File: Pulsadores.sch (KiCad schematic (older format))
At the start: 14 parts, among them SW1 Izquierda, SW2 Arriba, SW3 Abajo, SW4 Derecha, U6 74HC148

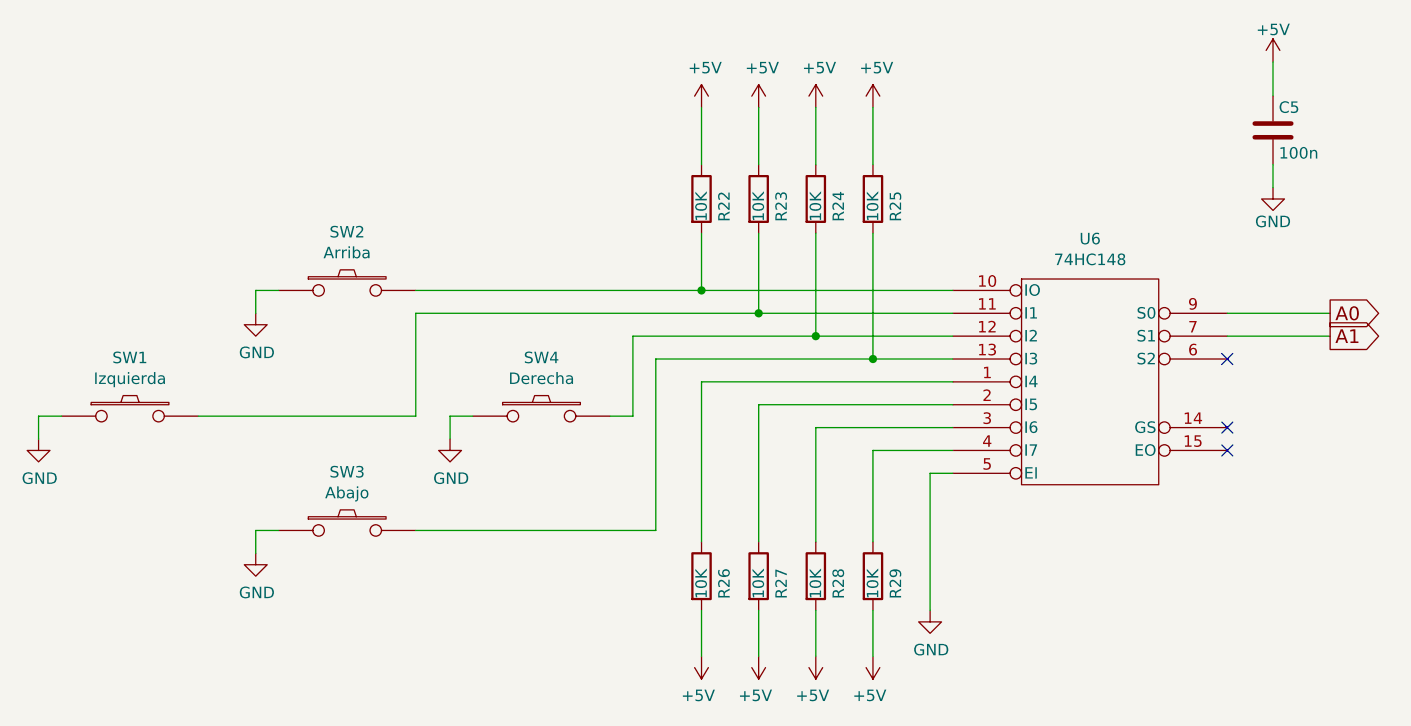
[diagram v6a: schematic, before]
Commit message: añadidos driver para led y conectores para fotodiodos infrarrojos
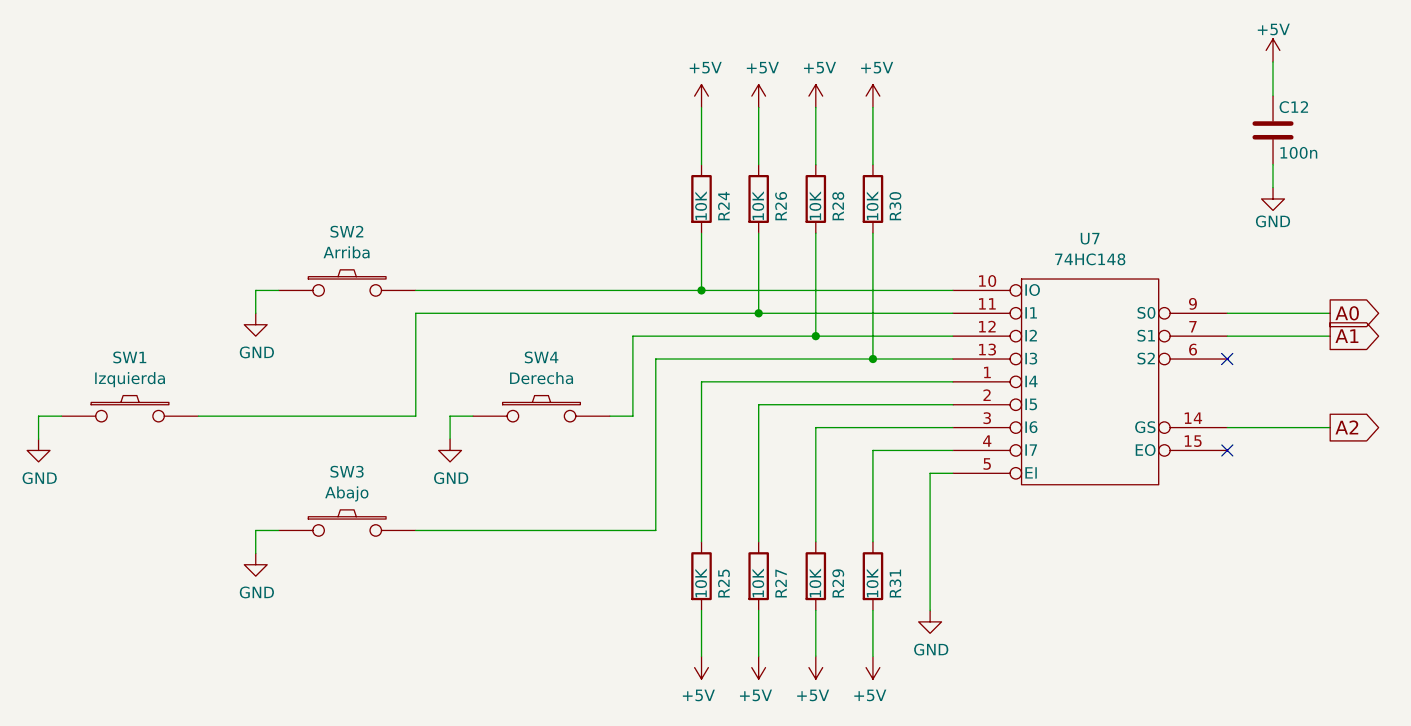
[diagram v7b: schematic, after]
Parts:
- renumbered C5 to C12, R22 to R24, R26 to R25, R23 to R26, R24 to R28, R28 to R29, R25 to R30, R29 to R31, U6 to U7
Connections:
- net A2: now reaches U7.14 (GS)
- no-connect marks 3 -> 2
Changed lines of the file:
@@
 EESchema Schematic File Version 2
+LIBS:Interfaces
+LIBS:Nano_PB-rescue
 LIBS:Sensores
 LIBS:power
@@
 LIBS:valves
 LIBS:MyLibrary
+LIBS:matriz_led
 LIBS:Nano_PB-cache
-EELAYER 25 0
+EELAYER 26 0
 EELAYER END
 $Descr User 8268 5846
 encoding utf-8
-Sheet 11 15
+Sheet 11 16
 Title "Bloque de pulsadores"
-Date "2016-08-07"
-Rev "V.0.2"
+Date "2017-01-04"
+Rev "V.0.3"
 Comp "NanoPlayBoard"
 Comment1 "Creada por Antonio Morales"
@@
 $EndDescr
 $Comp
-L 74LS148 U6
+L 74LS148 U7
 U 1 1 5793F705
 P 5650 2450
-F 0 "U6" H 5650 3075 50  0000 C CNN
+F 0 "U7" H 5650 3075 50  0000 C CNN
 F 1 "74HC148" H 5650 2984 50  0000 C CNN
 F 2 "Housings_SOIC:SOIC-16_3.9x9.9mm_Pitch1.27mm" H 5650 2450 50  0001 C CNN
@@
 	1050 2600 1050 2700
 $Comp
-L GND #PWR030
+L GND #PWR051
 U 1 1 57951274
 P 1050 2700
-F 0 "#PWR030" H 1050 2450 50  0001 C CNN
+F 0 "#PWR051" H 1050 2450 50  0001 C CNN
 F 1 "GND" H 1055 2527 50  0000 C CNN
 F 2 "" H 1050 2700 50  0000 C CNN
@@
 	2000 3100 2000 3200
 $Comp
-L GND #PWR031
+L GND #PWR052
 U 1 1 579512A4
 P 2000 3200
-F 0 "#PWR031" H 2000 2950 50  0001 C CNN
+F 0 "#PWR052" H 2000 2950 50  0001 C CNN
 F 1 "GND" H 2005 3027 50  0000 C CNN
 F 2 "" H 2000 3200 50  0000 C CNN
@@
 	2000 2050 2000 2150
 $Comp
-L GND #PWR032
+L GND #PWR053
 U 1 1 579512CF
 P 2000 2150
-F 0 "#PWR032" H 2000 1900 50  0001 C CNN
+F 0 "#PWR053" H 2000 1900 50  0001 C CNN
 F 1 "GND" H 2005 1977 50  0000 C CNN
 F 2 "" H 2000 2150 50  0000 C CNN
@@
 	2850 2600 2850 2700
 $Comp
-L GND #PWR033
+L GND #PWR054
 U 1 1 5795130B
 P 2850 2700
-F 0 "#PWR033" H 2850 2450 50  0001 C CNN
+F 0 "#PWR054" H 2850 2450 50  0001 C CNN
 F 1 "GND" H 2855 2527 50  0000 C CNN
 F 2 "" H 2850 2700 50  0000 C CNN
@@
 	2700 3100 3750 3100
 $Comp
-L R R22
+L R R24
 U 1 1 57951783
 P 3950 1650
-F 0 "R22" V 4050 1550 50  0000 L CNN
+F 0 "R24" V 4050 1550 50  0000 L CNN
 F 1 "10K" V 3950 1550 50  0000 L CNN
 F 2 "Resistencias:R_0805" V 3880 1650 50  0001 C CNN
@@
 $EndComp
 $Comp
-L R R23
+L R R26
 U 1 1 579517BD
 P 4200 1650
-F 0 "R23" V 4300 1550 50  0000 L CNN
+F 0 "R26" V 4300 1550 50  0000 L CNN
 F 1 "10K" V 4200 1550 50  0000 L CNN
 F 2 "Resistencias:R_0805" V 4130 1650 50  0001 C CNN
@@
 $EndComp
 $Comp
-L R R24
+L R R28
 U 1 1 579517EC
 P 4450 1650
-F 0 "R24" V 4550 1550 50  0000 L CNN
+F 0 "R28" V 4550 1550 50  0000 L CNN
 F 1 "10K" V 4450 1550 50  0000 L CNN
 F 2 "Resistencias:R_0805" V 4380 1650 50  0001 C CNN
@@
 $EndComp
 $Comp
-L R R25
+L R R30
 U 1 1 5795181A
 P 4700 1650
-F 0 "R25" V 4800 1550 50  0000 L CNN
+F 0 "R30" V 4800 1550 50  0000 L CNN
 F 1 "10K" V 4700 1550 50  0000 L CNN
 F 2 "Resistencias:R_0805" V 4630 1650 50  0001 C CNN
@@
 	3950 1500 3950 1250
 $Comp
-L +5V #PWR034
+L +5V #PWR055
 U 1 1 5795193F
 P 3950 1250
-F 0 "#PWR034" H 3950 1100 50  0001 C CNN
+F 0 "#PWR055" H 3950 1100 50  0001 C CNN
 F 1 "+5V" H 3965 1423 50  0000 C CNN
 F 2 "" H 3950 1250 50  0000 C CNN
@@
 $EndComp
 $Comp
-L +5V #PWR035
+L +5V #PWR056
 U 1 1 5795196C
 P 4200 1250
-F 0 "#PWR035" H 4200 1100 50  0001 C CNN
+F 0 "#PWR056" H 4200 1100 50  0001 C CNN
 F 1 "+5V" H 4215 1423 50  0000 C CNN
 F 2 "" H 4200 1250 50  0000 C CNN
@@
 $EndComp
 $Comp
-L +5V #PWR036
+L +5V #PWR057
 U 1 1 57951992
 P 4450 1250
-F 0 "#PWR036" H 4450 1100 50  0001 C CNN
+F 0 "#PWR057" H 4450 1100 50  0001 C CNN
 F 1 "+5V" H 4465 1423 50  0000 C CNN
 F 2 "" H 4450 1250 50  0000 C CNN
@@
 $EndComp
 $Comp
-L +5V #PWR037
+L +5V #PWR058
 U 1 1 579519B8
 P 4700 1250
-F 0 "#PWR037" H 4700 1100 50  0001 C CNN
+F 0 "#PWR058" H 4700 1100 50  0001 C CNN
 F 1 "+5V" H 4715 1423 50  0000 C CNN
 F 2 "" H 4700 1250 50  0000 C CNN
@@
 Wire Wire Line
 	4200 1250 4200 1500
-NoConn ~ 6250 2650
 NoConn ~ 6250 2750
 Wire Wire Line
@@
 Text GLabel 6700 2250 2    60   Output ~ 0
 A1
-NoConn ~ 6250 2350
-$Comp
-L R R26
+$Comp
+L R R25
 U 1 1 579521A8
 P 3950 3300
-F 0 "R26" V 4050 3200 50  0000 L CNN
+F 0 "R25" V 4050 3200 50  0000 L CNN
 F 1 "10K" V 3950 3200 50  0000 L CNN
 F 2 "Resistencias:R_0805" V 3880 3300 50  0001 C CNN
@@
 $EndComp
 $Comp
-L R R28
+L R R29
 U 1 1 57952253
 P 4450 3300
-F 0 "R28" V 4550 3200 50  0000 L CNN
+F 0 "R29" V 4550 3200 50  0000 L CNN
 F 1 "10K" V 4450 3200 50  0000 L CNN
 F 2 "Resistencias:R_0805" V 4380 3300 50  0001 C CNN
@@
 $EndComp
 $Comp
-L R R29
+L R R31
 U 1 1 5795229D
 P 4700 3300
-F 0 "R29" V 4800 3200 50  0000 L CNN
+F 0 "R31" V 4800 3200 50  0000 L CNN
 F 1 "10K" V 4700 3200 50  0000 L CNN
 F 2 "Resistencias:R_0805" V 4630 3300 50  0001 C CNN
@@
 	3950 3450 3950 3650
 $Comp
-L +5V #PWR038
+L +5V #PWR059
 U 1 1 579524C5
 P 3950 3650
-F 0 "#PWR038" H 3950 3500 50  0001 C CNN
+F 0 "#PWR059" H 3950 3500 50  0001 C CNN
 F 1 "+5V" H 3965 3823 50  0000 C CNN
 F 2 "" H 3950 3650 50  0000 C CNN
@@
 $EndComp
 $Comp
-L +5V #PWR039
+L +5V #PWR060
 U 1 1 57952518
 P 4200 3650
-F 0 "#PWR039" H 4200 3500 50  0001 C CNN
+F 0 "#PWR060" H 4200 3500 50  0001 C CNN
 F 1 "+5V" H 4215 3823 50  0000 C CNN
 F 2 "" H 4200 3650 50  0000 C CNN
@@
 $EndComp
 $Comp
-L +5V #PWR040
+L +5V #PWR061
 U 1 1 5795254A
 P 4450 3650
-F 0 "#PWR040" H 4450 3500 50  0001 C CNN
+F 0 "#PWR061" H 4450 3500 50  0001 C CNN
 F 1 "+5V" H 4465 3823 50  0000 C CNN
 F 2 "" H 4450 3650 50  0000 C CNN
@@
 $EndComp
 $Comp
-L +5V #PWR041
+L +5V #PWR062
 U 1 1 5795257C
 P 4700 3650
-F 0 "#PWR041" H 4700 3500 50  0001 C CNN
+F 0 "#PWR062" H 4700 3500 50  0001 C CNN
 F 1 "+5V" H 4715 3823 50  0000 C CNN
 F 2 "" H 4700 3650 50  0000 C CNN
@@
 	4950 2850 4950 3450
 $Comp
-L GND #PWR042
+L GND #PWR063
 U 1 1 5795449C
 P 4950 3450
-F 0 "#PWR042" H 4950 3200 50  0001 C CNN
+F 0 "#PWR063" H 4950 3200 50  0001 C CNN
 F 1 "GND" H 4955 3277 50  0000 C CNN
 F 2 "" H 4950 3450 50  0000 C CNN
@@
 $EndComp
 $Comp
-L C C5
+L C C12
 U 1 1 57993D3A
 P 6450 1350
-F 0 "C5" H 6475 1450 50  0000 L CNN
+F 0 "C12" H 6475 1450 50  0000 L CNN
 F 1 "100n" H 6475 1250 50  0000 L CNN
 F 2 "Capacitors_SMD:C_0805" H 6488 1200 50  0001 C CNN
@@
 $EndComp
 $Comp
-L GND #PWR043
+L GND #PWR064
 U 1 1 57993D41
 P 6450 1600
-F 0 "#PWR043" H 6450 1350 50  0001 C CNN
+F 0 "#PWR064" H 6450 1350 50  0001 C CNN
 F 1 "GND" H 6450 1450 50  0000 C CNN
 F 2 "" H 6450 1600 50  0000 C CNN
@@
 $EndComp
 $Comp
-L +5V #PWR044
+L +5V #PWR065
 U 1 1 57993D47
 P 6450 1050
-F 0 "#PWR044" H 6450 900 50  0001 C CNN
+F 0 "#PWR065" H 6450 900 50  0001 C CNN
 F 1 "+5V" H 6450 1190 50  0000 C CNN
 F 2 "" H 6450 1050 50  0000 C CNN
@@
 50 17 92 01 51 92 64 0C CE 27 7B 4E 87 A3 FC C9 E9 39 BC D0 3B DC 1F CF E6 3C 60 30 83 10 3D 18
 F4 0B 89 52 73 00 8B 80 91 08 28 22 8F 6D AB AA BD D3 E7 C4 3E A7 59 B4 A9 94 4D 1C A1 84 52 AC
-9A 46 F6 7A E1 FF 00 F0 A4 0C 74 26 CB 7B D1 00 00 00 00 49 45 4E 44 AE 42 60 82 00
+9A 46 F6 7A E1 FF 00 F0 A4 0C 74 26 CB 7B D1 00 00 00 00 49 45 4E 44 AE 42 60 82
 EndData
 $EndBitmap
+Wire Wire Line
+	6250 2650 6700 2650
+Text GLabel 6700 2650 2    60   Output ~ 0
+A2
+NoConn ~ 6250 2350
 $EndSCHEMATC
